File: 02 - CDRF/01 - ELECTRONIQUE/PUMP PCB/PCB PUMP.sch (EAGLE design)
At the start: 13 parts, among them J3 PWRPAD2-5MM, J4 PWRPAD2-5MM, Q1 FDN360P, Q2 FDN360P

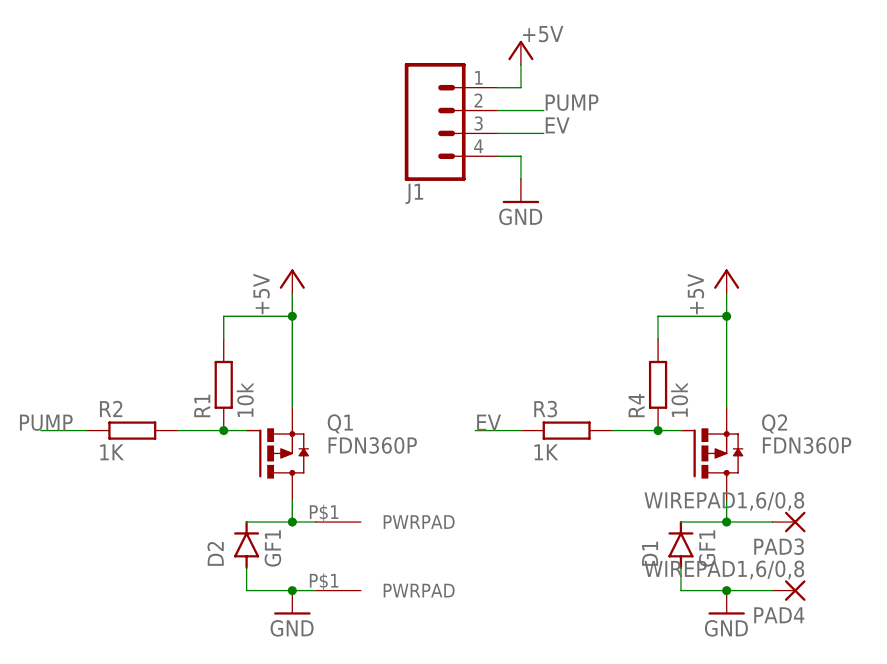
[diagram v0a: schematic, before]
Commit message: Update
Change P-MOSFET by N-MOSFET
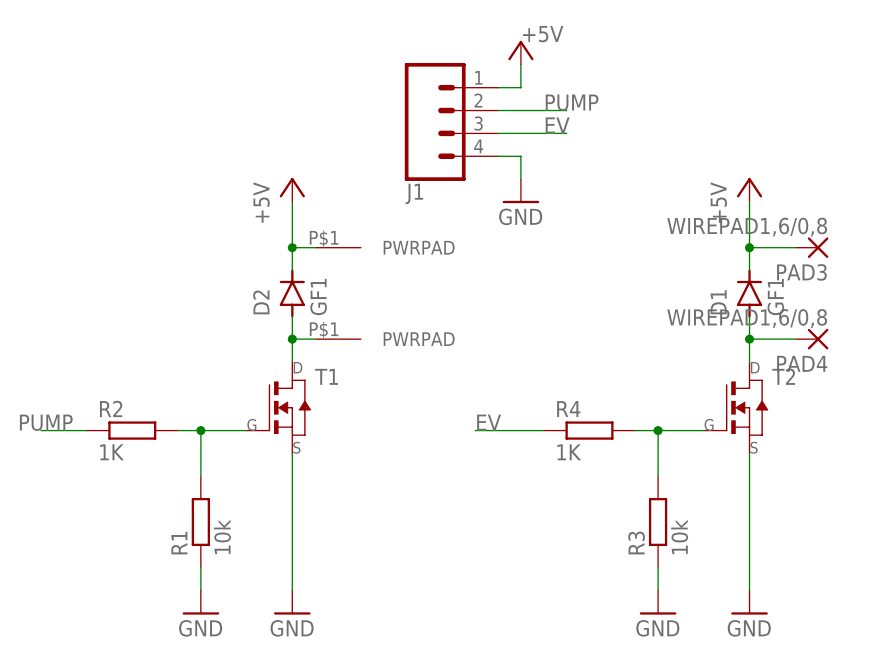
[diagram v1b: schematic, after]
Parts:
- removed Q1, Q2: FDN360P, transistor-power:FDN360P
- added T1, T2: (no value), fab:NMOSFETSOT23
- R3: value 1K -> 10k
- R4: value 10k -> 1K
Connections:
- removed net N$5: D2.C, J3.PWRPAD, Q1.D
- removed net N$8: D1.C, PAD3.P, Q2.D
- new net N$2: D2.A, J3.PWRPAD, T1.D
- new net N$3: R1.2, R2.2, T1.G
- net +5V: now also D1.C, D2.C, J4.PWRPAD, PAD3.P; no longer Q1.S, Q2.S, R1.2, R4.2
- net EV: now also R4.1; no longer R3.1
- net GND: now also R1.1, R3.1, T1.S, T2.S; no longer D1.A, D2.A, J4.PWRPAD, PAD4.P
- net N$1: now also D1.A, PAD4.P, T2.D; no longer Q2.G, R3.2, R4.1
- net N$4: now also R3.2, R4.2, T2.G; no longer Q1.G, R1.1, R2.2
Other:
- moved on the sheet: D1, D2, PAD3, PAD4, R1, R3, R4
